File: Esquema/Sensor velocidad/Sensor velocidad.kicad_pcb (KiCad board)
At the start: 2 copper layers, 47 parts, among them J1 DB9_Female_MountingHoles, J2 DB9_Male_MountingHoles, J3 DB9_Female_MountingHoles, J4 DB9_Male_MountingHoles, U1 TCRT5000_GD, U2 TCRT5000_GD

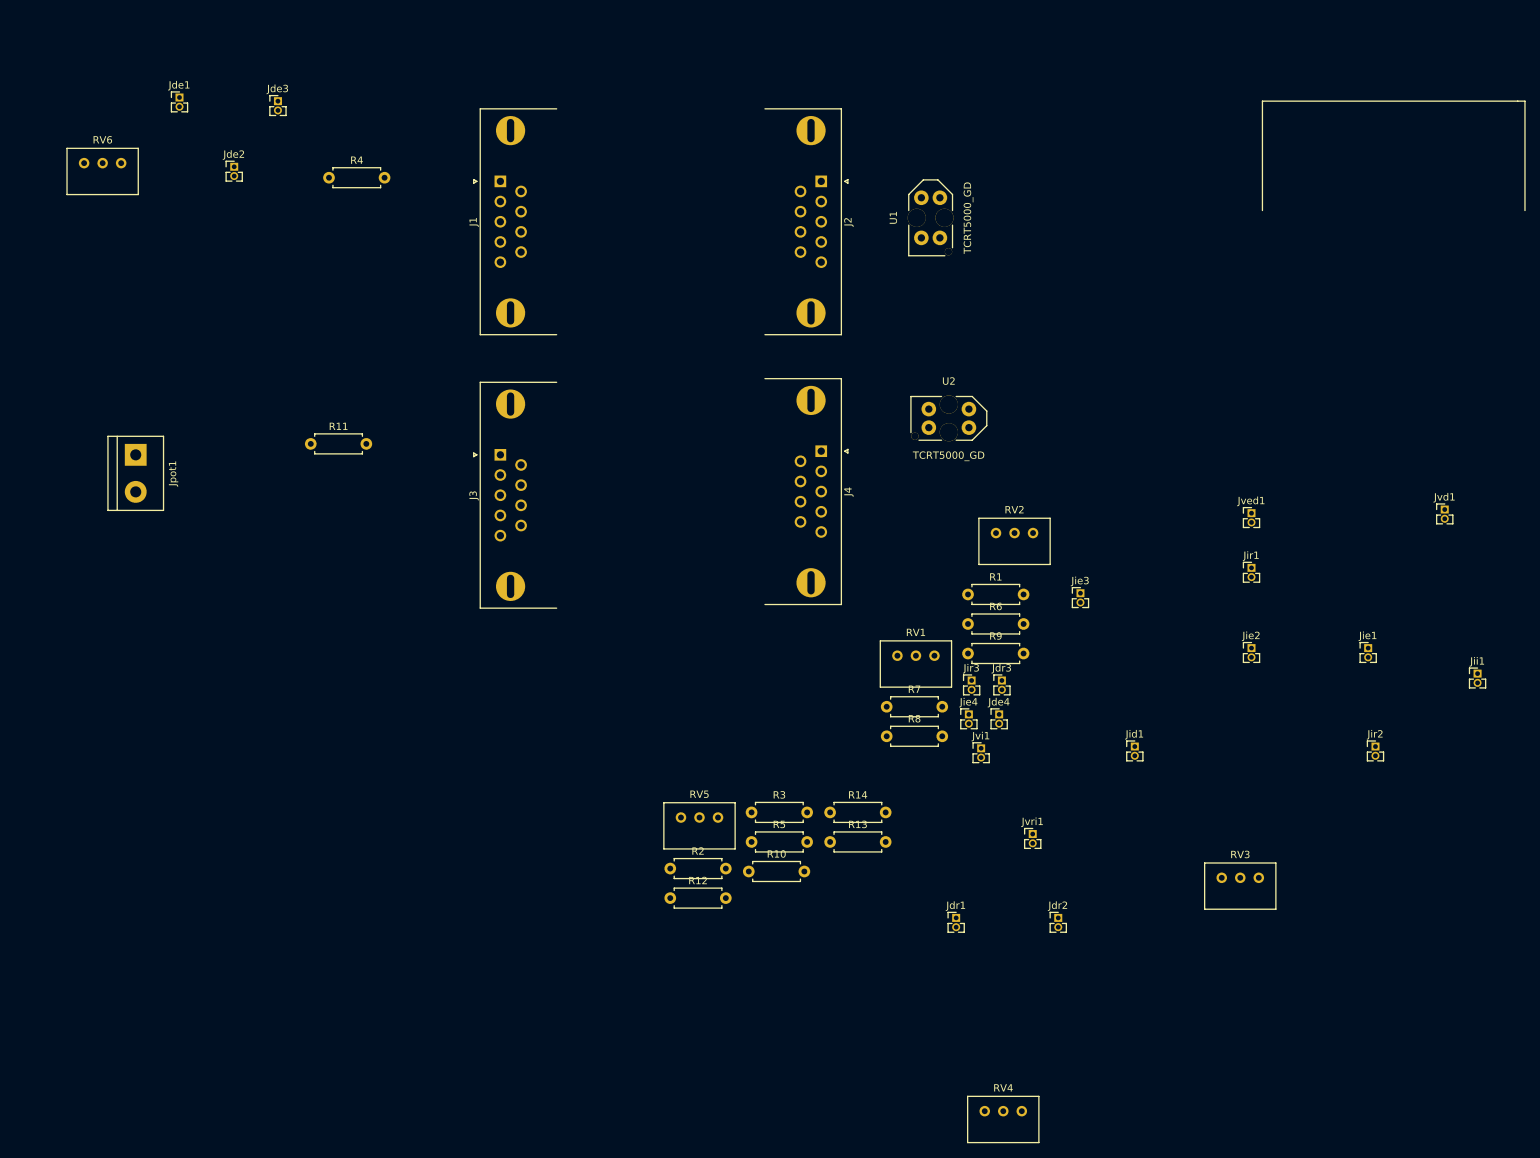
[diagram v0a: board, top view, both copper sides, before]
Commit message: Acomodé los componentes de las placas de sensado derecho.
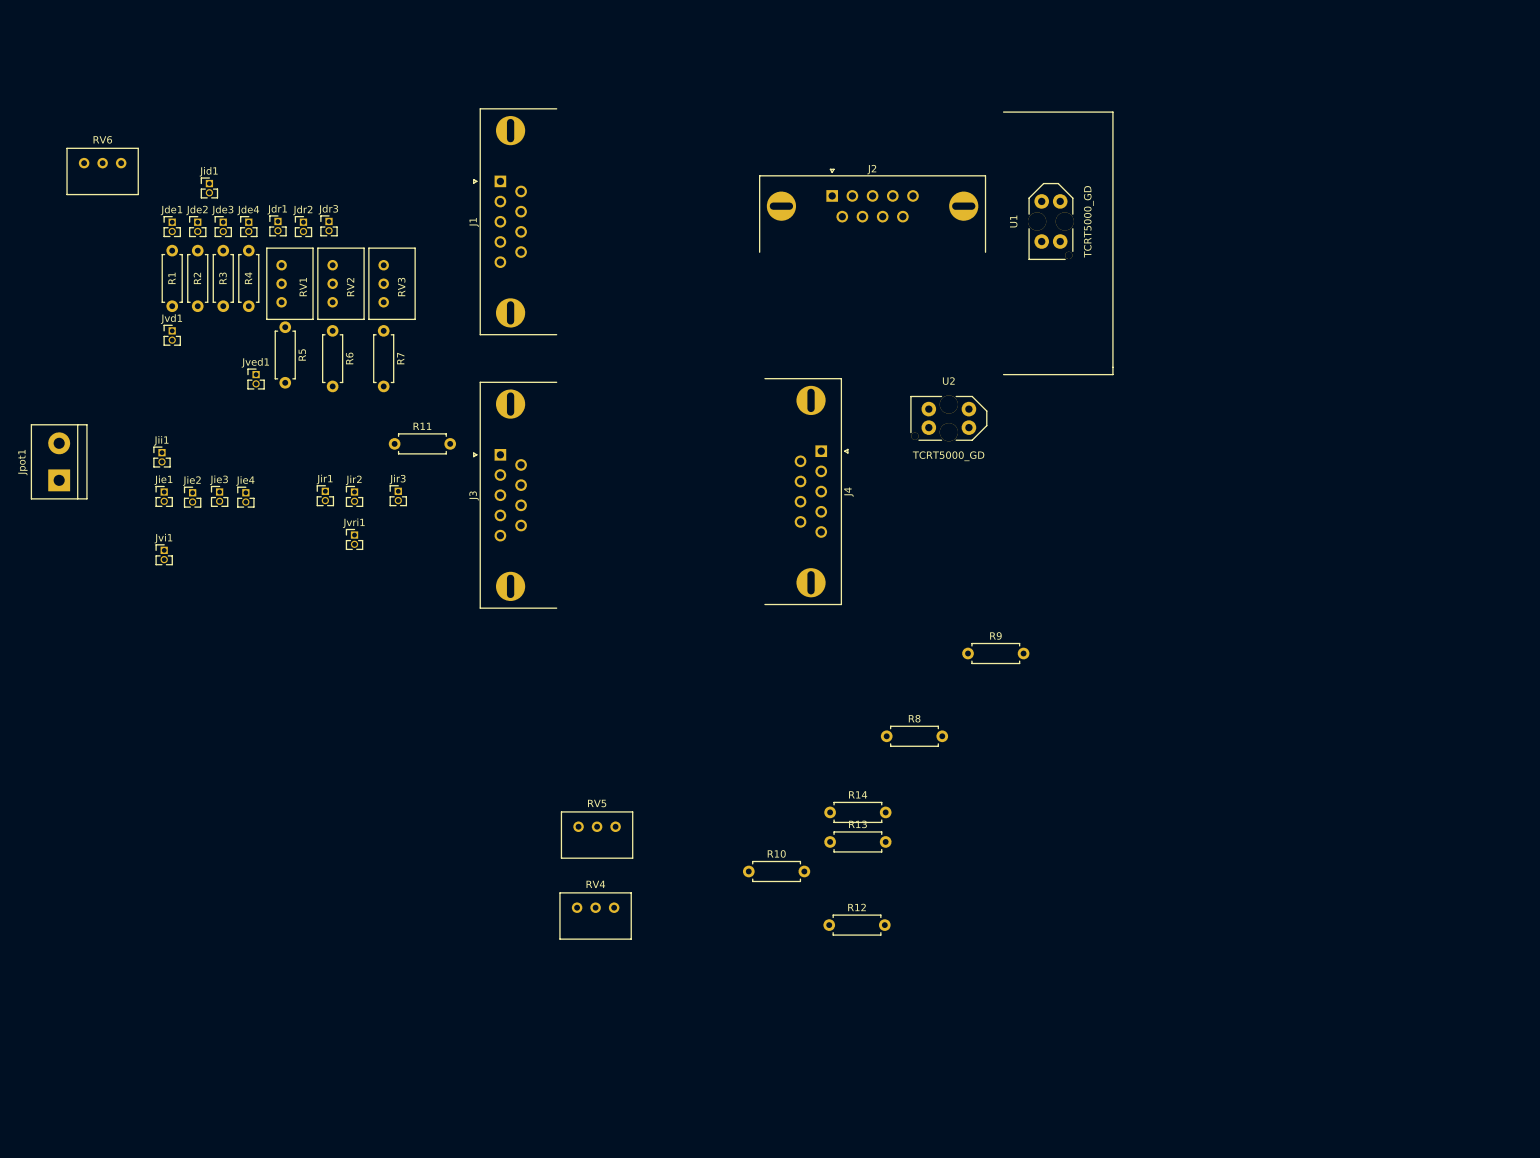
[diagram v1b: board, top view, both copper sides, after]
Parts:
- moved Jii1 182.9 mm to (39.1, 77.7)
- moved Jvd1 176.2 mm to (40.5, 61.0)
- moved Jie1 166.5 mm to (39.4, 83.1)
- moved Jid1 148.5 mm to (45.6, 40.8)
- moved Jie2 146.8 mm to (43.3, 83.2)
- moved RV3 146.5 mm to (69.5, 52.0), turned to 90 degrees
- moved Jir2 144.3 mm to (65.5, 83.1)
- moved Jdr2 140.8 mm to (58.5, 46.1)
- moved Jved1 137.8 mm to (52.0, 67.0)
- moved Jdr1 133.3 mm to (55.0, 46.0)
- moved Jir1 127.4 mm to (61.5, 83.0)
- moved Jde4 123.1 mm to (51.0, 46.1)
- moved R1 118.9 mm to (40.5, 50.0), turned to 270 degrees
- moved Jie3 118.9 mm to (47.0, 83.1)
- moved Jvi1 115.3 mm to (39.4, 91.1)
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
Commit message: Terminé de acomodar a grandes rasgos los componentes
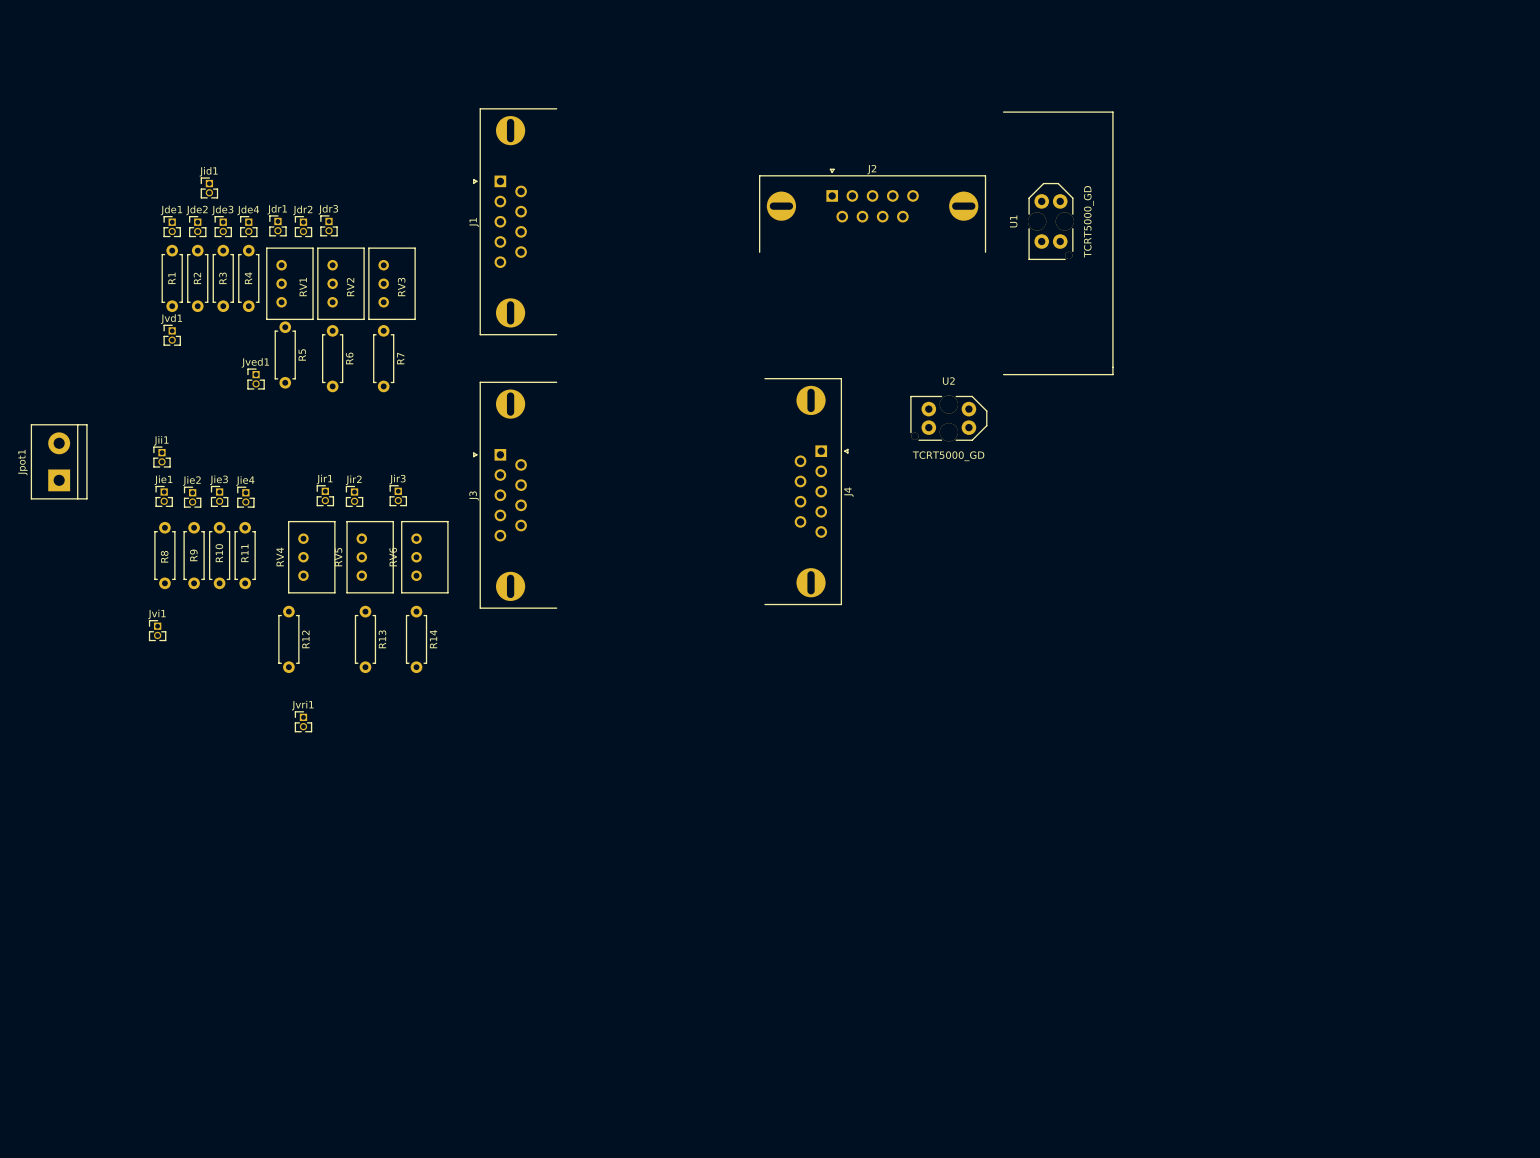
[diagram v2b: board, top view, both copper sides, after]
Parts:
- moved R9 107.5 mm to (43.5, 88.0), turned to 270 degrees
- moved R8 103.0 mm to (39.5, 88.0), turned to 270 degrees
- moved R10 86.5 mm to (47.0, 88.0), turned to 270 degrees
- moved R12 85.7 mm to (56.5, 99.5), turned to 270 degrees
- moved R13 71.1 mm to (67.0, 99.5), turned to 270 degrees
- moved RV4 66.1 mm to (58.5, 89.5), turned to 90 degrees
- moved RV6 65.5 mm to (74.0, 89.5), turned to 90 degrees
- moved R14 63.0 mm to (74.0, 99.5), turned to 270 degrees
- moved RV5 52.6 mm to (66.5, 89.5), turned to 90 degrees
- moved Jvri1 26.0 mm to (58.5, 114.0)
- moved R11 23.5 mm to (50.5, 88.0), turned to 270 degrees
- moved Jvi1 10.4 mm to (38.5, 101.5)

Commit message: Avance de placa, queda acomodar puntos de medición
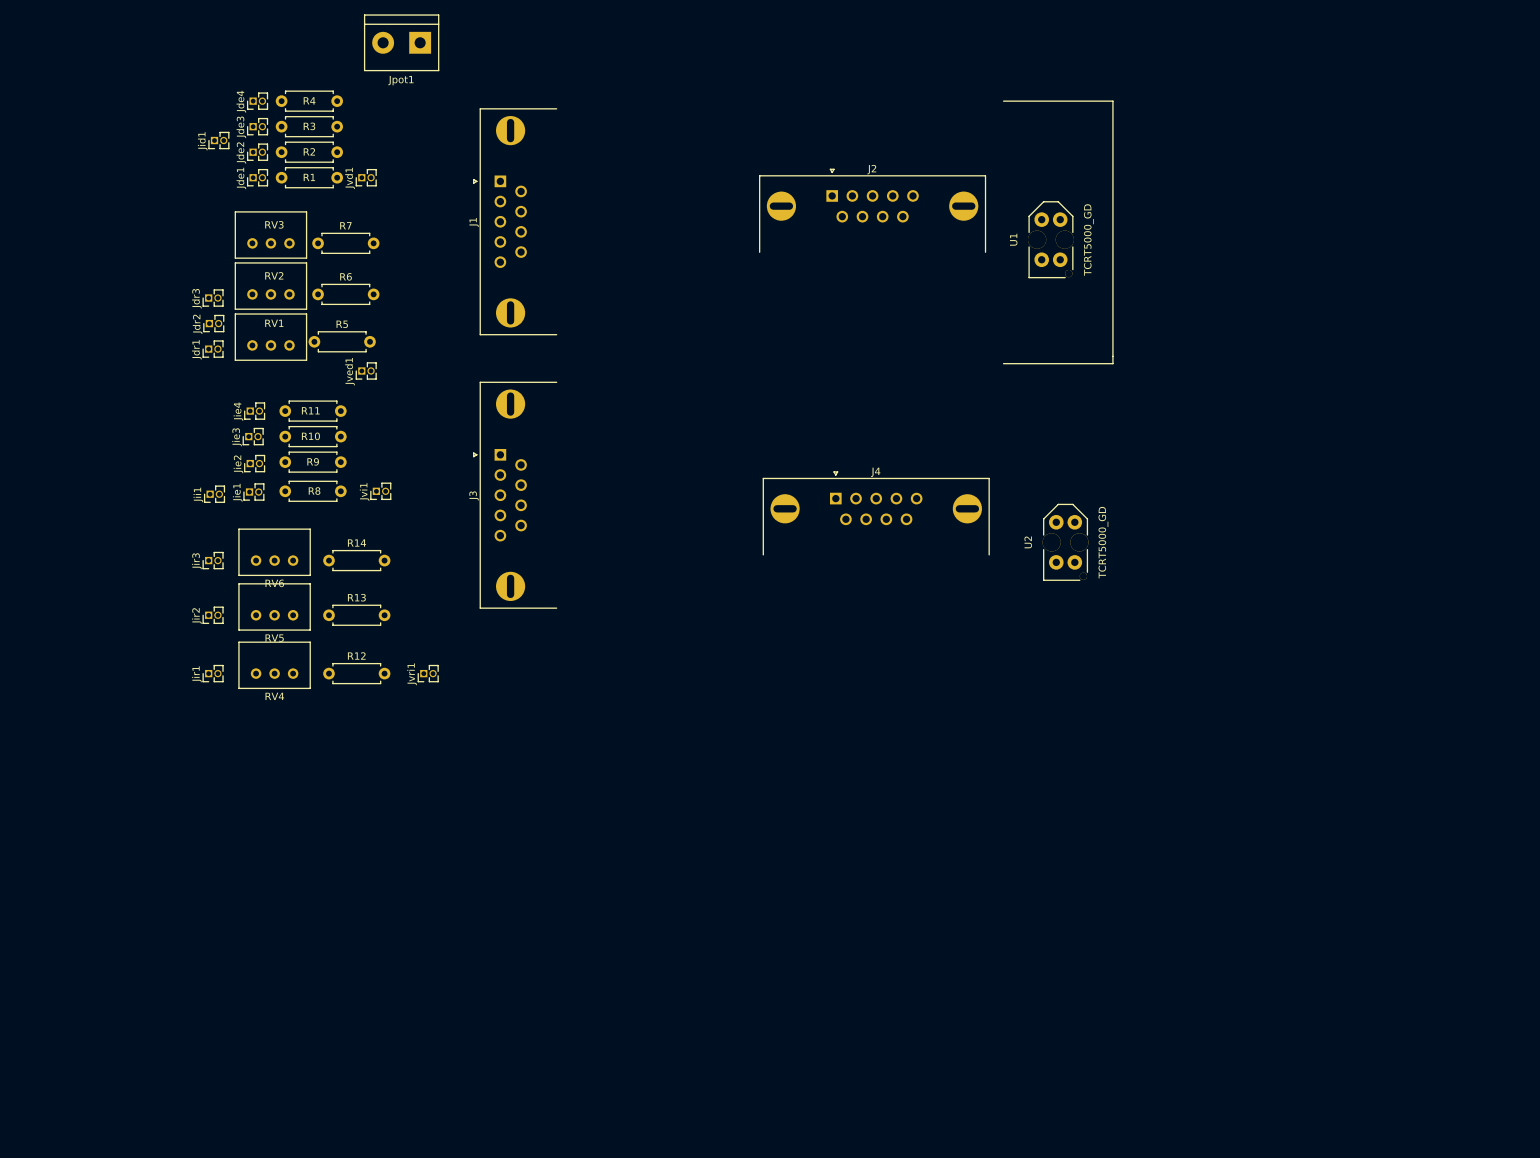
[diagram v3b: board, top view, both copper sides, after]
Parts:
- moved Jpot1 77.8 mm to (74.5, 21.5), turned to 180 degrees
- moved Jvi1 35.2 mm to (68.5, 83.0), turned to 90 degrees
- moved Jvd1 33.4 mm to (66.5, 40.0), turned to 90 degrees
- moved Jir1 29.7 mm to (45.5, 108.0), turned to 90 degrees
- moved Jir3 27.7 mm to (45.5, 92.5), turned to 90 degrees
- moved Jir2 26.2 mm to (45.5, 100.0), turned to 90 degrees
- moved U2 23.3 mm to (163.0, 90.0), turned to 90 degrees
- moved RV6 22.2 mm to (52.0, 92.5), turned to 180 degrees
- moved R4 21.0 mm to (55.5, 29.5), turned to 0 degrees
- moved Jdr1 19.9 mm to (45.5, 63.5), turned to 90 degrees
- moved RV4 19.6 mm to (52.0, 108.0), turned to 180 degrees
- moved Jdr3 19.6 mm to (45.5, 56.5), turned to 90 degrees
- moved Jdr2 19.0 mm to (45.6, 60.0), turned to 90 degrees
- moved R3 18.8 mm to (55.5, 33.0), turned to 0 degrees
- moved RV3 18.2 mm to (51.5, 49.0), turned to 180 degrees
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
